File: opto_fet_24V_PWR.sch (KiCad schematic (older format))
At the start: 0 parts

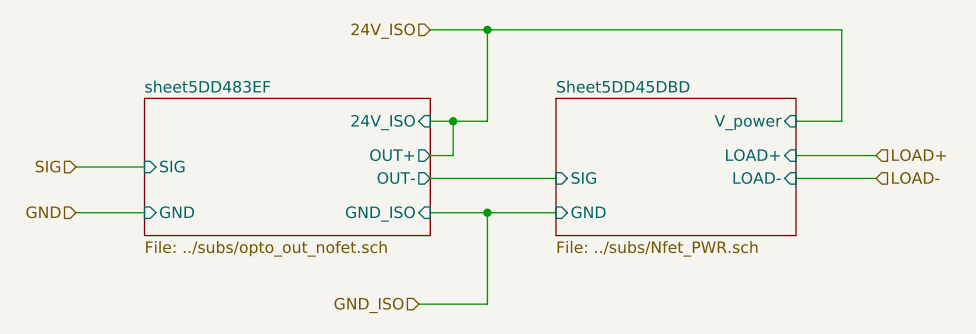
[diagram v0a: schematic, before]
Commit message: modified opto-isolated NFET schematic - needed PU resistor
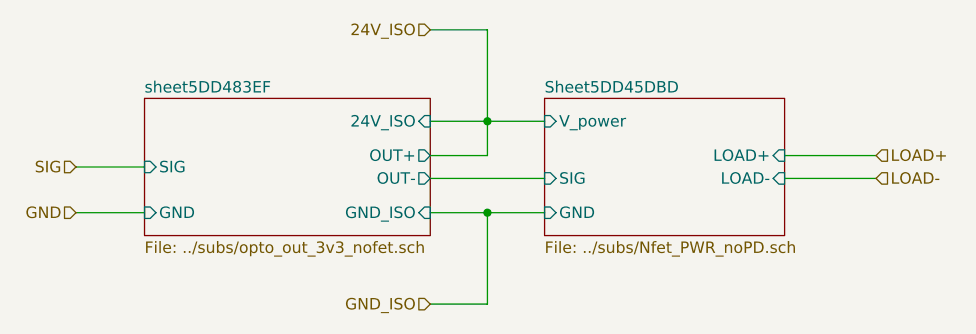
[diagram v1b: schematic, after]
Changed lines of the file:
@@
 $Descr A4 11693 8268
 encoding utf-8
-Sheet 16 18
+Sheet 8 18
 Title ""
 Date ""
@@
 $EndDescr
 $Sheet
-S 6050 2400 1050 600
-U 5DD45DBE
-F0 "Sheet5DD45DBD" 50
-F1 "../subs/Nfet_PWR.sch" 50
-F2 "SIG" I L 6050 2750 50
-F3 "GND" I L 6050 2900 50
-F4 "LOAD-" I R 7100 2750 50
-F5 "LOAD+" I R 7100 2650 50
-F6 "V_power" I R 7100 2500 50
-$EndSheet
-$Sheet
 S 4250 2400 1250 600
 U 5DD483EF
 F0 "sheet5DD483EF" 50
-F1 "../subs/opto_out_nofet.sch" 50
+F1 "../subs/opto_out_3v3_nofet.sch" 50
 F2 "SIG" I L 4250 2700 50
 F3 "24V_ISO" I R 5500 2500 50
@@
 $EndSheet
 Wire Wire Line
-	5500 2650 5600 2650
+	5500 2650 5750 2650
 Wire Wire Line
-	5600 2650 5600 2500
+	5750 2650 5750 2500
 Wire Wire Line
-	5600 2500 5500 2500
+	5750 2500 5500 2500
 Wire Wire Line
 	5500 2900 5750 2900
@@
 Text HLabel 3950 2700 0    50   Input ~ 0
 SIG
-Text HLabel 5500 2100 0    50   Input ~ 0
-24V_ISO
-Text HLabel 5450 3300 0    50   Input ~ 0
+Text HLabel 5500 3300 0    50   Input ~ 0
 GND_ISO
 Text HLabel 7450 2650 2    50   Input ~ 0
@@
 LOAD-
 Wire Wire Line
-	7450 2650 7100 2650
+	7450 2650 7050 2650
 Wire Wire Line
-	7100 2750 7450 2750
+	7050 2750 7450 2750
 Wire Wire Line
 	5750 2100 5750 2500
+Connection ~ 5750 2500
 Wire Wire Line
-	5750 2500 5600 2500
-Connection ~ 5600 2500
-Wire Wire Line
-	5500 2100 5750 2100
-Wire Wire Line
-	5750 2100 7300 2100
-Wire Wire Line
-	7300 2100 7300 2500
-Wire Wire Line
-	7300 2500 7100 2500
-Connection ~ 5750 2100
-Wire Wire Line
-	5500 2750 6050 2750
-Wire Wire Line
-	5450 3300 5750 3300
+	5500 3300 5750 3300
 Wire Wire Line
 	5750 3300 5750 2900
 Connection ~ 5750 2900
 Wire Wire Line
-	5750 2900 6050 2900
+	5750 2900 6000 2900
 Wire Wire Line
 	3950 2900 4250 2900
 Wire Wire Line
 	3950 2700 4250 2700
+Wire Wire Line
+	5500 2100 5750 2100
+Text HLabel 5500 2100 0    50   Input ~ 0
+24V_ISO
+Wire Wire Line
+	6000 2500 5750 2500
+Wire Wire Line
+	5500 2750 6000 2750
+$Sheet
+S 6000 2400 1050 600
+U 5DD45DBE
+F0 "Sheet5DD45DBD" 50
+F1 "../subs/Nfet_PWR_noPD.sch" 50
+F2 "SIG" I L 6000 2750 50
+F3 "GND" I L 6000 2900 50
+F4 "LOAD-" I R 7050 2750 50
+F5 "LOAD+" I R 7050 2650 50
+F6 "V_power" I L 6000 2500 50
+$EndSheet
 $EndSCHEMATC
